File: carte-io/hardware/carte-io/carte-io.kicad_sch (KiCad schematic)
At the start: 0 parts

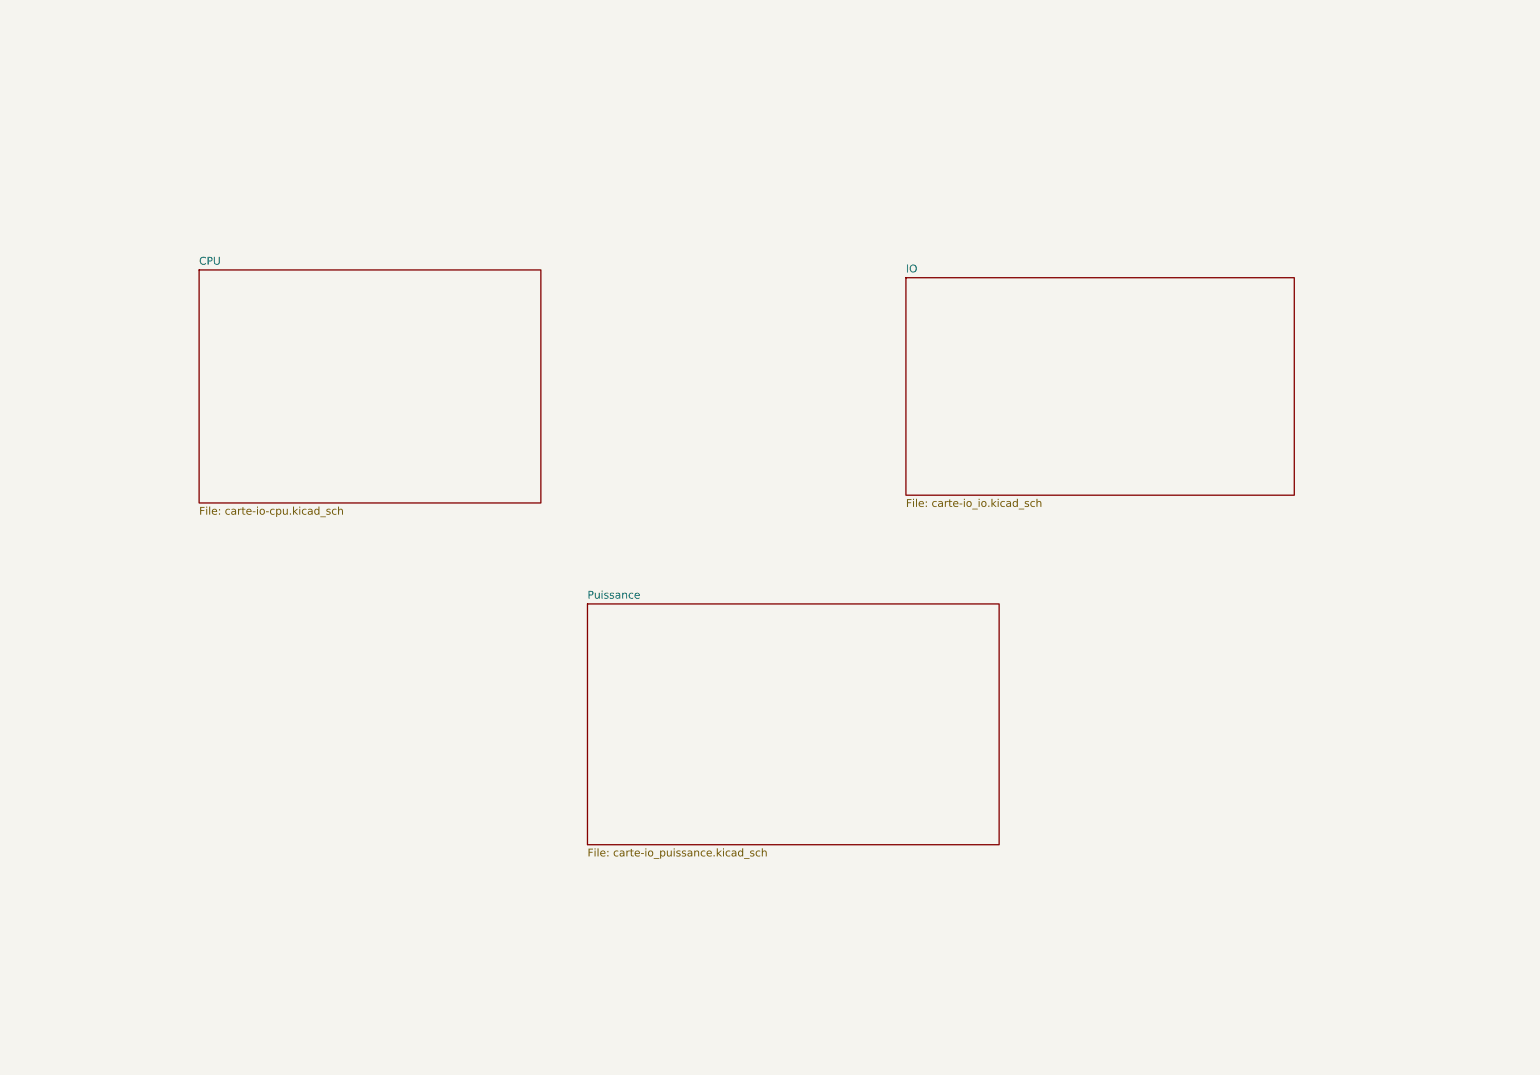
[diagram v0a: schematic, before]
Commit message: Evolution du schema de la carte IO + creation du projet STM32CubeIDE
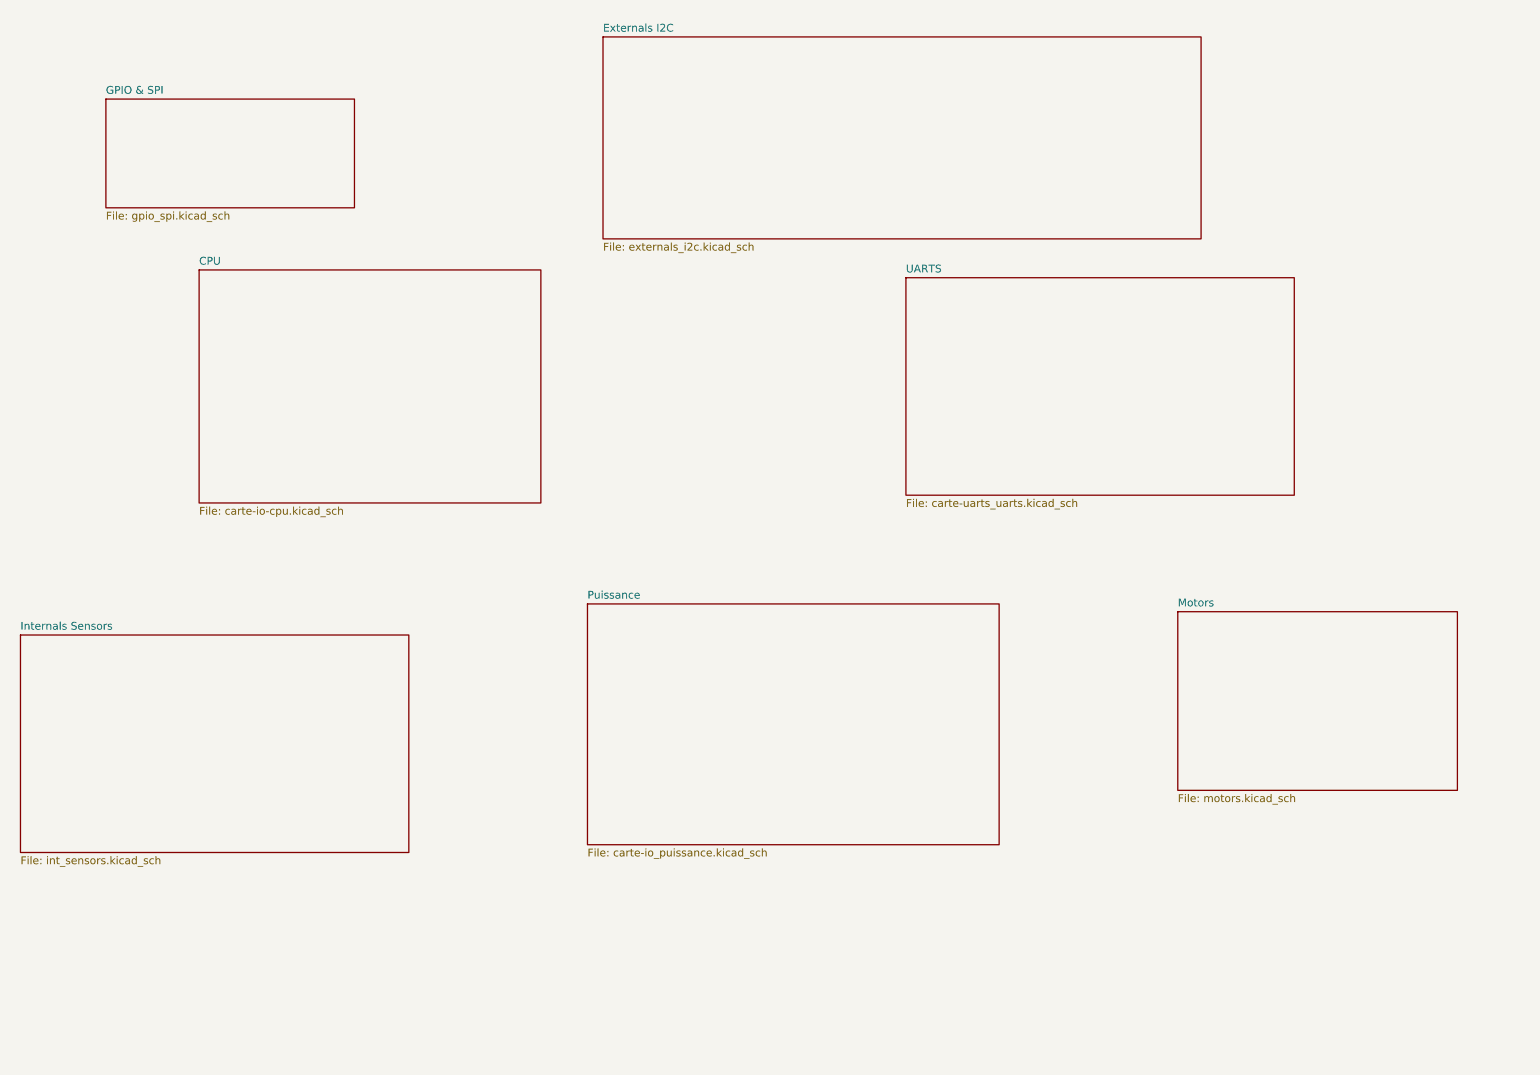
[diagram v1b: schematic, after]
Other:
- sheet IO renamed UARTS
- added sheet Externals I2C (externals_i2c.kicad_sch)
- added sheet GPIO & SPI (gpio_spi.kicad_sch)
- added sheet Internals Sensors (int_sensors.kicad_sch)
- added sheet Motors (motors.kicad_sch)
- sheet UARTS: file carte-io_io.kicad_sch -> carte-uarts_uarts.kicad_sch
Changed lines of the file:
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@@
+	)
+	(sheet
+		(at 217.17 118.11)
+		(size 45.72 29.21)
+		(fields_autoplaced yes)
+		(stroke
+			(width 0.1524)
+			(type solid)
+		)
+		(fill
+			(color 0 0 0 0.0000)
+		)
+		(property "Sheetname" "Motors"
+			(at 217.17 117.3984 0)
+			(effects
+				(font
+					(size 1.27 1.27)
+				)
+				(justify left bottom)
+			)
+		)
+		(property "Sheetfile" "motors.kicad_sch"
+			(at 217.17 147.9046 0)
+			(effects
+				(font
+					(size 1.27 1.27)
+				)
+				(justify left top)
+			)
+		)
+		(instances
+			(project "carte-io"
+				(path "/acbeee85-bee7-482c-b859-0ad6bf15d6be"
+					(page "5")
+				)
+			)
+		)
+	)
+	(sheet
+		(at 41.91 34.29)
+		(size 40.64 17.78)
+		(fields_autoplaced yes)
+		(stroke
+			(width 0.1524)
+			(type solid)
+		)
+		(fill
+			(color 0 0 0 0.0000)
+		)
+		(property "Sheetname" "GPIO & SPI"
+			(at 41.91 33.5784 0)
+			(effects
+				(font
+					(size 1.27 1.27)
+				)
+				(justify left bottom)
+			)
+		)
+		(property "Sheetfile" "gpio_spi.kicad_sch"
+			(at 41.91 52.6546 0)
+			(effects
+				(font
+					(size 1.27 1.27)
+				)
+				(justify left top)
+			)
+		)
+		(instances
+			(project "carte-io"
+				(path "/acbeee85-bee7-482c-b859-0ad6bf15d6be"
+					(page "8")
+				)
+			)
+		)
 	)
 	(sheet
@@
 			(project "carte-io"
 				(path "/acbeee85-bee7-482c-b859-0ad6bf15d6be"
-					(page "4")
+					(page "3")
+				)
+			)
+		)
+	)
+	(sheet
+		(at 27.94 121.92)
+		(size 63.5 35.56)
+		(fields_autoplaced yes)
+		(stroke
+			(width 0.1524)
+			(type solid)
+		)
+		(fill
+			(color 0 0 0 0.0000)
+		)
+		(property "Sheetname" "Internals Sensors"
+			(at 27.94 121.2084 0)
+			(effects
+				(font
+					(size 1.27 1.27)
+				)
+				(justify left bottom)
+			)
+		)
+		(property "Sheetfile" "int_sensors.kicad_sch"
+			(at 27.94 158.0646 0)
+			(effects
+				(font
+					(size 1.27 1.27)
+				)
+				(justify left top)
+			)
+		)
+		(instances
+			(project "carte-io"
+				(path "/acbeee85-bee7-482c-b859-0ad6bf15d6be"
+					(page "6")
+				)
+			)
+		)
+	)
+	(sheet
+		(at 123.19 24.13)
+		(size 97.79 33.02)
+		(fields_autoplaced yes)
+		(stroke
+			(width 0.1524)
+			(type solid)
+		)
+		(fill
+			(color 0 0 0 0.0000)
+		)
+		(property "Sheetname" "Externals I2C"
+			(at 123.19 23.4184 0)
+			(effects
+				(font
+					(size 1.27 1.27)
+				)
+				(justify left bottom)
+			)
+		)
+		(property "Sheetfile" "externals_i2c.kicad_sch"
+			(at 123.19 57.7346 0)
+			(effects
+				(font
+					(size 1.27 1.27)
+				)
+				(justify left top)
+			)
+		)
+		(instances
+			(project "carte-io"
+				(path "/acbeee85-bee7-482c-b859-0ad6bf15d6be"
+					(page "7")
 				)
 			)
@@
 			(color 0 0 0 0.0000)
 		)
-		(property "Sheetname" "IO"
+		(property "Sheetname" "UARTS"
 			(at 172.72 62.7884 0)
 			(effects
@@
 			)
 		)
-		(property "Sheetfile" "carte-io_io.kicad_sch"
+		(property "Sheetfile" "carte-uarts_uarts.kicad_sch"
 			(at 172.72 99.6446 0)
 			(effects
@@
 			(project "carte-io"
 				(path "/acbeee85-bee7-482c-b859-0ad6bf15d6be"
-					(page "3")
-				)
-			)
+					(page "4")
+				)
+			)

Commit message: Carte IO routée version 1
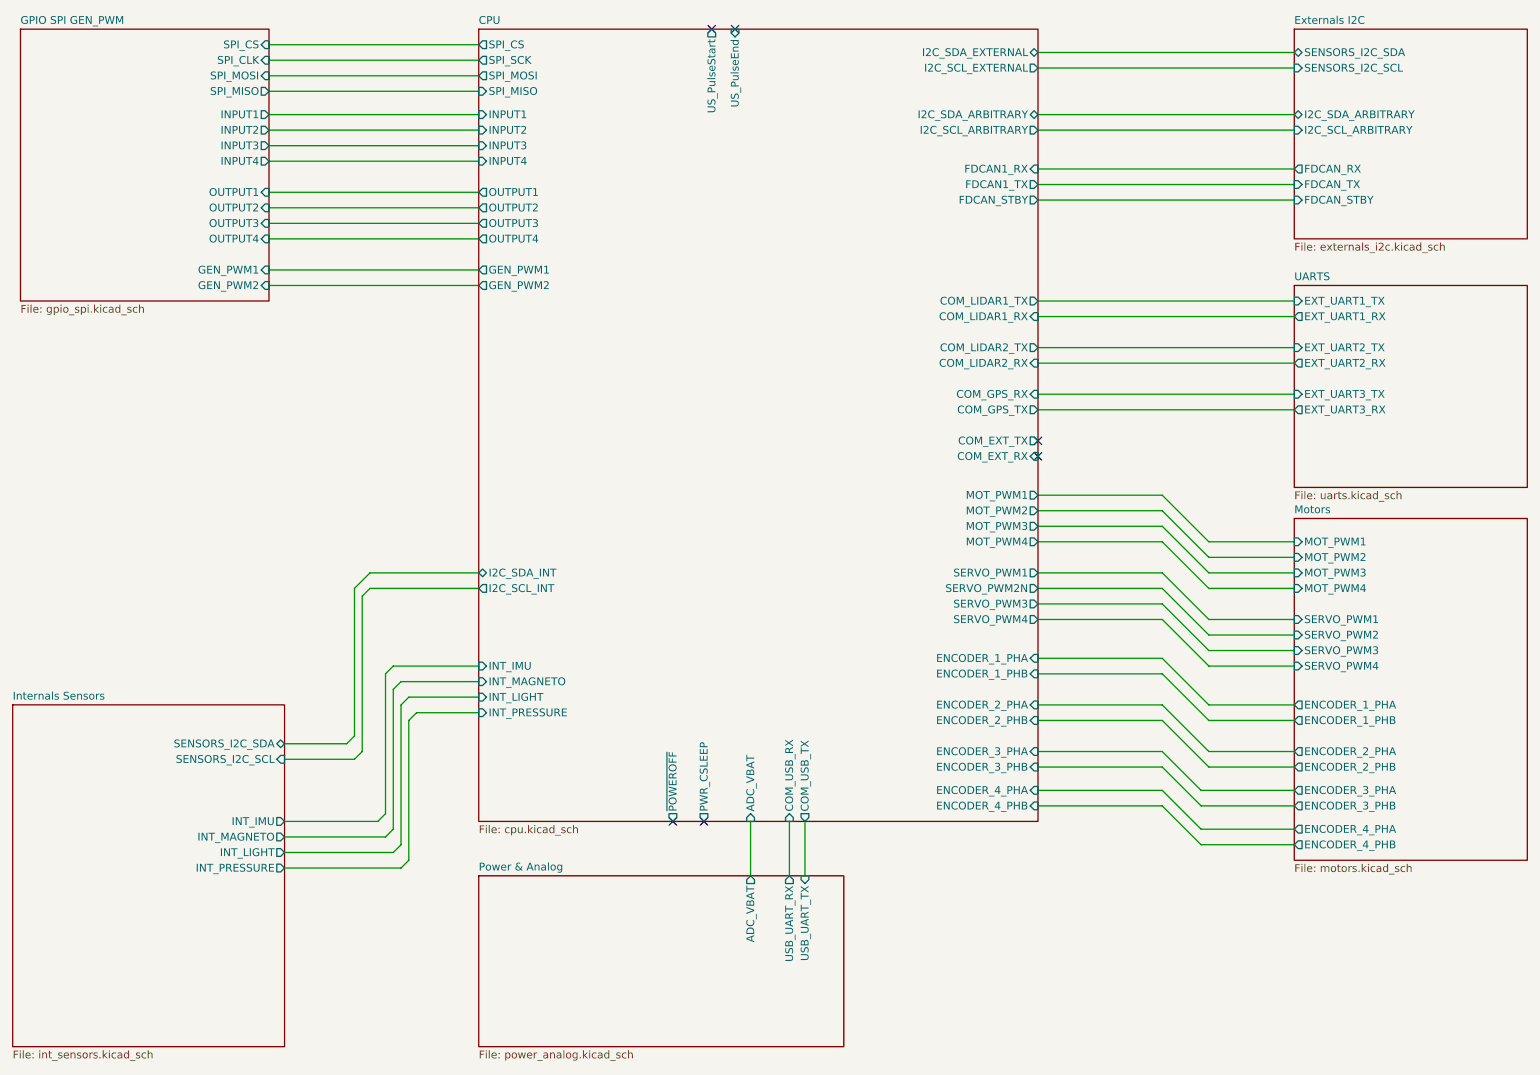
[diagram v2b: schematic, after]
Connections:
- no-connect marks 0 -> 6
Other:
- sheet GPIO & SPI renamed GPIO SPI GEN_PWM
- sheet Puissance renamed Power & Analog
- sheet CPU: file carte-io-cpu.kicad_sch -> cpu.kicad_sch
- sheet CPU ports: added ADC_VBAT, COM_EXT_RX, COM_EXT_TX, COM_GPS_RX, COM_GPS_TX, COM_LIDAR1_RX, COM_LIDAR1_TX, COM_LIDAR2_RX, COM_LIDAR2_TX, COM_USB_RX, COM_USB_TX, ENCODER_1_PHA, ENCODER_1_PHB, ENCODER_2_PHA, ENCODER_2_PHB, ENCODER_3_PHA, ENCODER_3_PHB, ENCODER_4_PHA, ENCODER_4_PHB, FDCAN1_RX, FDCAN1_TX, FDCAN_STBY, GEN_PWM1, GEN_PWM2, I2C_SCL_ARBITRARY, I2C_SCL_EXTERNAL, I2C_SCL_INT, I2C_SDA_ARBITRARY, I2C_SDA_EXTERNAL, I2C_SDA_INT, INPUT1, INPUT2, INPUT3, INPUT4, INT_IMU, INT_LIGHT, INT_MAGNETO, INT_PRESSURE, MOT_PWM1, MOT_PWM2, MOT_PWM3, MOT_PWM4, OUTPUT1, OUTPUT2, OUTPUT3, OUTPUT4, PWR_CSLEEP, SERVO_PWM1, SERVO_PWM2N, SERVO_PWM3, SERVO_PWM4, SPI_CS, SPI_MISO, SPI_MOSI, SPI_SCK, US_PulseEnd, US_PulseStart, ~{POWEROFF}; removed none
- sheet Externals I2C ports: added FDCAN_RX, FDCAN_STBY, FDCAN_TX, I2C_SCL_ARBITRARY, I2C_SDA_ARBITRARY, SENSORS_I2C_SCL, SENSORS_I2C_SDA; removed none
- sheet GPIO SPI GEN_PWM ports: added GEN_PWM1, GEN_PWM2, INPUT1, INPUT2, INPUT3, INPUT4, OUTPUT1, OUTPUT2, OUTPUT3, OUTPUT4, SPI_CLK, SPI_CS, SPI_MISO, SPI_MOSI; removed none
- sheet Internals Sensors ports: added INT_IMU, INT_LIGHT, INT_MAGNETO, INT_PRESSURE, SENSORS_I2C_SCL, SENSORS_I2C_SDA; removed none
- sheet Motors ports: added ENCODER_1_PHA, ENCODER_1_PHB, ENCODER_2_PHA, ENCODER_2_PHB, ENCODER_3_PHA, ENCODER_3_PHB, ENCODER_4_PHA, ENCODER_4_PHB, MOT_PWM1, MOT_PWM2, MOT_PWM3, MOT_PWM4, SERVO_PWM1, SERVO_PWM2, SERVO_PWM3, SERVO_PWM4; removed none
- sheet Power & Analog: file carte-io_puissance.kicad_sch -> power_analog.kicad_sch
- sheet Power & Analog ports: added ADC_VBAT, USB_UART_RX, USB_UART_TX; removed none
- sheet UARTS: file carte-uarts_uarts.kicad_sch -> uarts.kicad_sch
- sheet UARTS ports: added EXT_UART1_RX, EXT_UART1_TX, EXT_UART2_RX, EXT_UART2_TX, EXT_UART3_RX, EXT_UART3_TX; removed none

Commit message: Carte version 1.1 terminée
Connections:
- no-connect marks 6 -> 4
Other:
- sheet CPU ports: added ADC_AN1, ADC_AN2, IO1, IO2, IO3, IO4; removed GEN_PWM1, GEN_PWM2, INPUT1, INPUT2, INPUT3, INPUT4, OUTPUT1, OUTPUT2, OUTPUT3, OUTPUT4, SPI_CS, SPI_MISO, SPI_MOSI, SPI_SCK
- sheet GPIO SPI GEN_PWM ports: added ADC_AN1, ADC_AN2, IN_OUT1, IN_OUT2, IN_OUT3, IN_OUT4; removed GEN_PWM1, GEN_PWM2, INPUT1, INPUT2, INPUT3, INPUT4, OUTPUT1, OUTPUT2, OUTPUT3, OUTPUT4, SPI_CLK, SPI_CS, SPI_MISO, SPI_MOSI
- sheet Power & Analog ports: added PWR_CSLEEP, ~{POWEROFF}; removed none
